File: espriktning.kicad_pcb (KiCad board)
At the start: 2 copper layers, 20 x 75 mm, 58 parts, among them J1 USB_C_Receptacle_USB2.0, J2 Conn_Sensor, J3 Conn_Fan, J4 Conn_01x08, Q1 2N7002K, Q2 S8050, Q3 S8050, SW1 Reset, SW2 Flash, U1 ESP-12F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

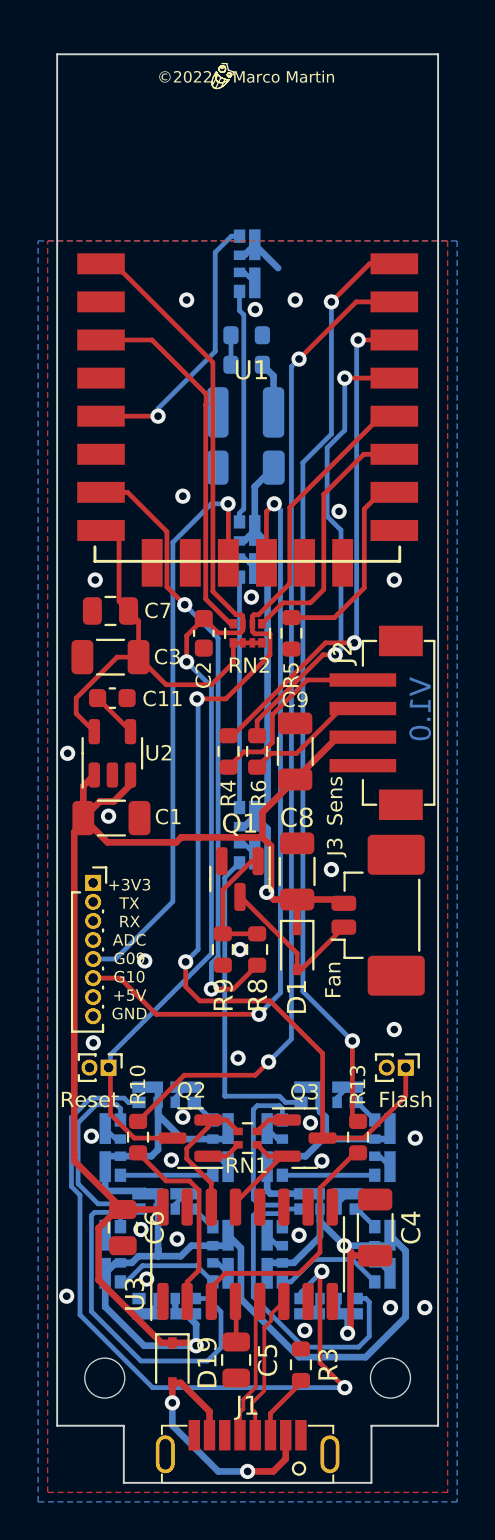
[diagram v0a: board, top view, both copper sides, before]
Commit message: relayout to actually fit
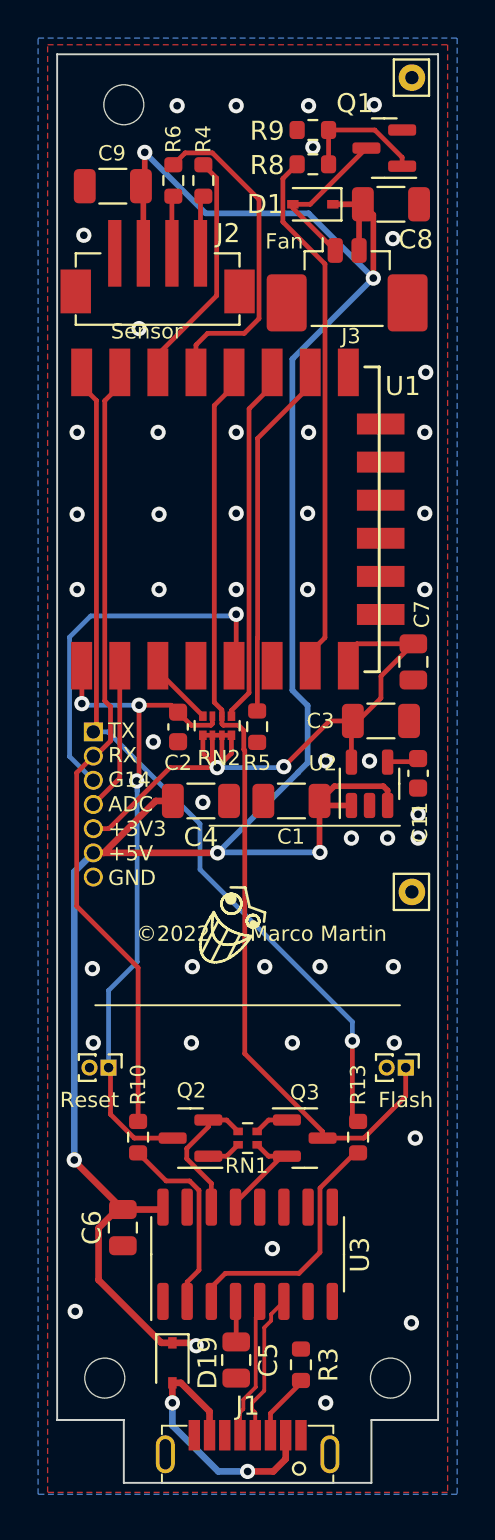
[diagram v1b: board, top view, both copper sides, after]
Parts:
- removed C10: 10u, Capacitor_SMD:C_1206_3216Metric
- removed D10, D11, D12, D13, D14, D15, D16, D17, D18, D2, D3, D4, D5, D6, D7, D8, D9: SK6812, espriktning:SK6812D-EC3210R
- removed R1: GT36528, Resistor_SMD:R_1210_3225Metric
- removed R2, R7: 12k, Resistor_SMD:R_0603_1608Metric
- added J6: Conn_01x01_Male, Connector_Pin:Pin_D0.7mm_L6.5mm_W1.8mm_FlatFork, F.Cu at (48.6, 74.0)
- added J7: Conn_01x01_Male, Connector_Pin:Pin_D0.7mm_L6.5mm_W1.8mm_FlatFork, F.Cu at (48.6, 31.2)
- added REF**: MountingHole_2.1mm, MountingHole:MountingHole_2.1mm, F.Cu at (33.5, 32.6)
- J4: footprint Connector_PinSocket_1.00mm:PinSocket_1x08_P1.00mm_Vertical -> Connector_PinSocket_1.27mm:PinSocket_1x07_P1.27mm_Vertical
- moved R9 43.3 mm to (43.4, 34.0), turned to 180 degrees
- moved R8 41.3 mm to (43.4, 35.8), turned to 180 degrees
- moved D1 39.1 mm to (43.4, 37.9), turned to 180 degrees
- moved Q1 39.1 mm to (47.2, 34.9), turned to 180 degrees
- moved C8 35.4 mm to (47.5, 37.9), turned to 0 degrees
- moved J3 33.7 mm to (45.2, 41.5), turned to 0 degrees
- moved C9 31.2 mm to (32.9, 36.9), turned to 180 degrees
- moved R6 30.3 mm to (36.1, 36.6)
- moved R4 30.0 mm to (37.7, 36.6)
- moved J2 26.1 mm to (35.3, 42.2), turned to 0 degrees
- moved C4 24.2 mm to (37.5, 69.2), turned to 0 degrees
- moved U1 20.5 mm to (31.3, 61.4), turned to 90 degrees
- moved C11 16.5 mm to (49.0, 67.8), turned to -90 degrees
- moved C7 16.1 mm to (48.7, 61.9), turned to -90 degrees
- moved C3 14.6 mm to (47.0, 65.0), turned to 0 degrees
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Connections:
- J4 pad 1: +3V3 -> TX
- J4 pad 2: TX -> RX
- J4 pad 3: RX -> GPIO14
- J4 pad 5: GPIO9 -> +3V3
- J4 pad 6: GPIO10 -> +5V
- J4 pad 7: +5V -> GND
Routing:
- net +5V: track 189.7 -> 122.6 mm, vias 4 -> 6
- net GPIO10: track 39.5 -> 0.00 mm, vias 2 -> 0
- net Net-(D11-Pad4): track 38.7 -> 0.00 mm, vias 2 -> 0
- net GPIO9: track 30.4 -> 0.00 mm, vias 1 -> 0
- net RST: track 58.1 -> 36.7 mm, vias 1 -> 3
- net Net-(D17-Pad4): track 19.0 -> 0.00 mm
- net GND: track 17.7 -> 0.00 mm, vias 30 -> 46
- net Net-(D4-Pad4): track 16.7 -> 0.00 mm
- net Net-(D10-Pad4): track 16.5 -> 0.00 mm
- net Net-(RN2-Pad4): track 18.8 -> 4.33 mm
- net +3V3: track 22.1 -> 36.4 mm, vias 0 -> 2
- net GPIO5: track 25.8 -> 13.2 mm, vias 2 -> 0
- net Net-(D2-Pad4): track 12.3 -> 0.00 mm
- net Net-(D3-Pad4): track 12.1 -> 0.00 mm
- net Net-(D14-Pad4): track 10.3 -> 0.00 mm
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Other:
- outline, holes or cut-outs redrawn
- board text added: "Sensor"
- board text added: "TX RX G14 ADC +3V3 +5V GND"
- board text removed: "+3V3 TX RX ADC G09 G10 +5V GND"
- board text removed: "Sens"
- board text removed: "V1.0"
